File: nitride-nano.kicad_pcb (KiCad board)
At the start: 2 copper layers, 213 parts, among them J1 DX07S024JJ2R1300, J2 61300411121, Q1 EPC2367, Q10 SQJB90EP-T1_GE3, Q11 AO3404A, Q2 EPC2367, Q3 EPC2367, Q4 EPC2367, Q6 AGM612AP, Q7 AO3404A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

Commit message: Fixed the library again
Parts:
- added J3: Conn_01x04_Pin, thommys-parts2:CONN-TH_XT90PW-M.G.Y, F.Cu at (83.0, 80.0)
- added U1: LT8390AIUFD-PBF, thommys-parts2:UFD_28_ADI, F.Cu at (100.8, 63.0)
- moved Q1 1.30 mm to (128.8, 48.8)
- moved Q4 1.30 mm to (128.8, 63.5)
- moved Q2 1.30 mm to (128.8, 53.7)
- moved Q3 1.30 mm to (128.8, 58.6)

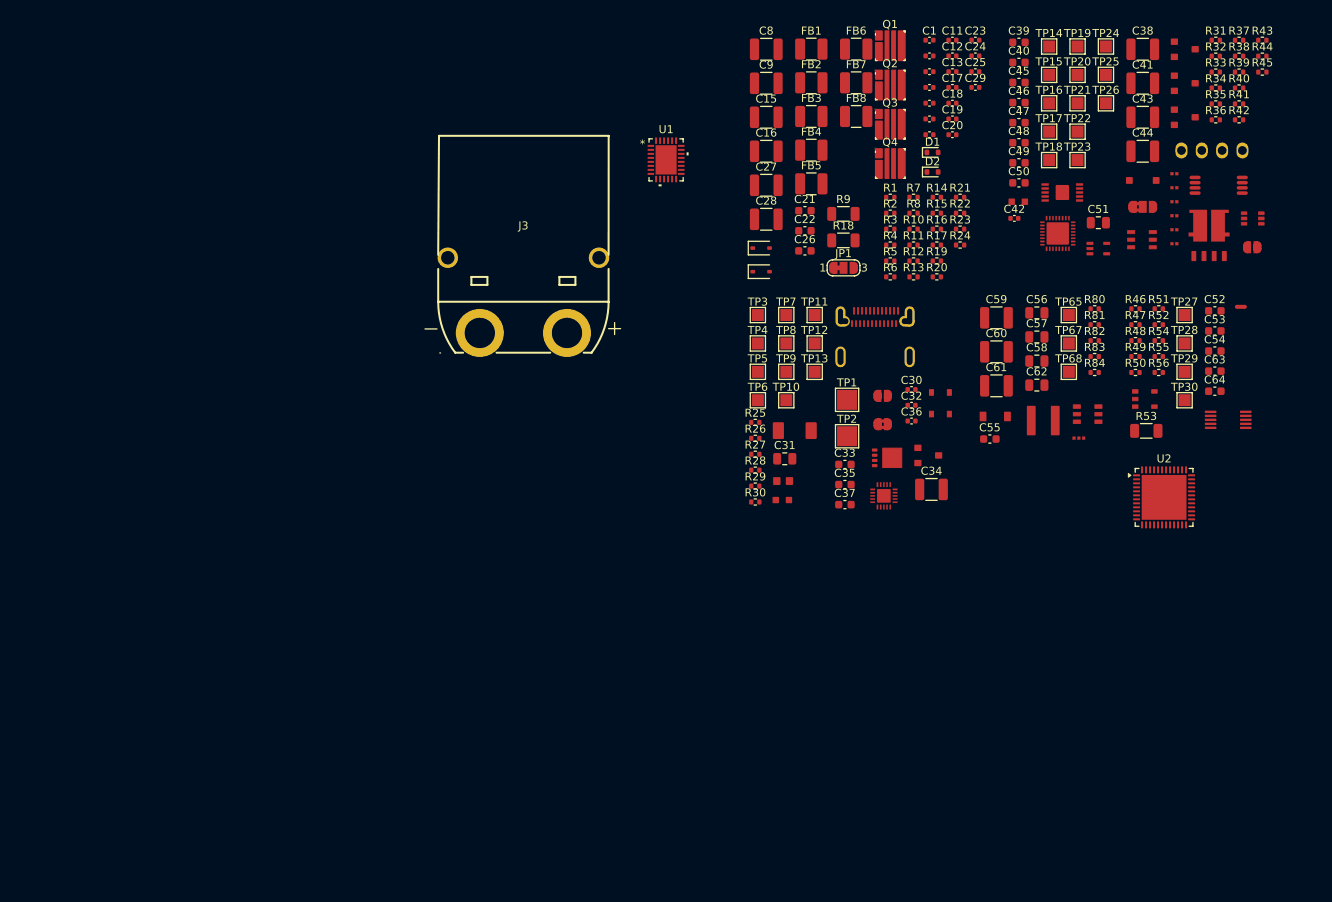
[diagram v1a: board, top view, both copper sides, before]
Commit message: Cleaned up the hierarchy
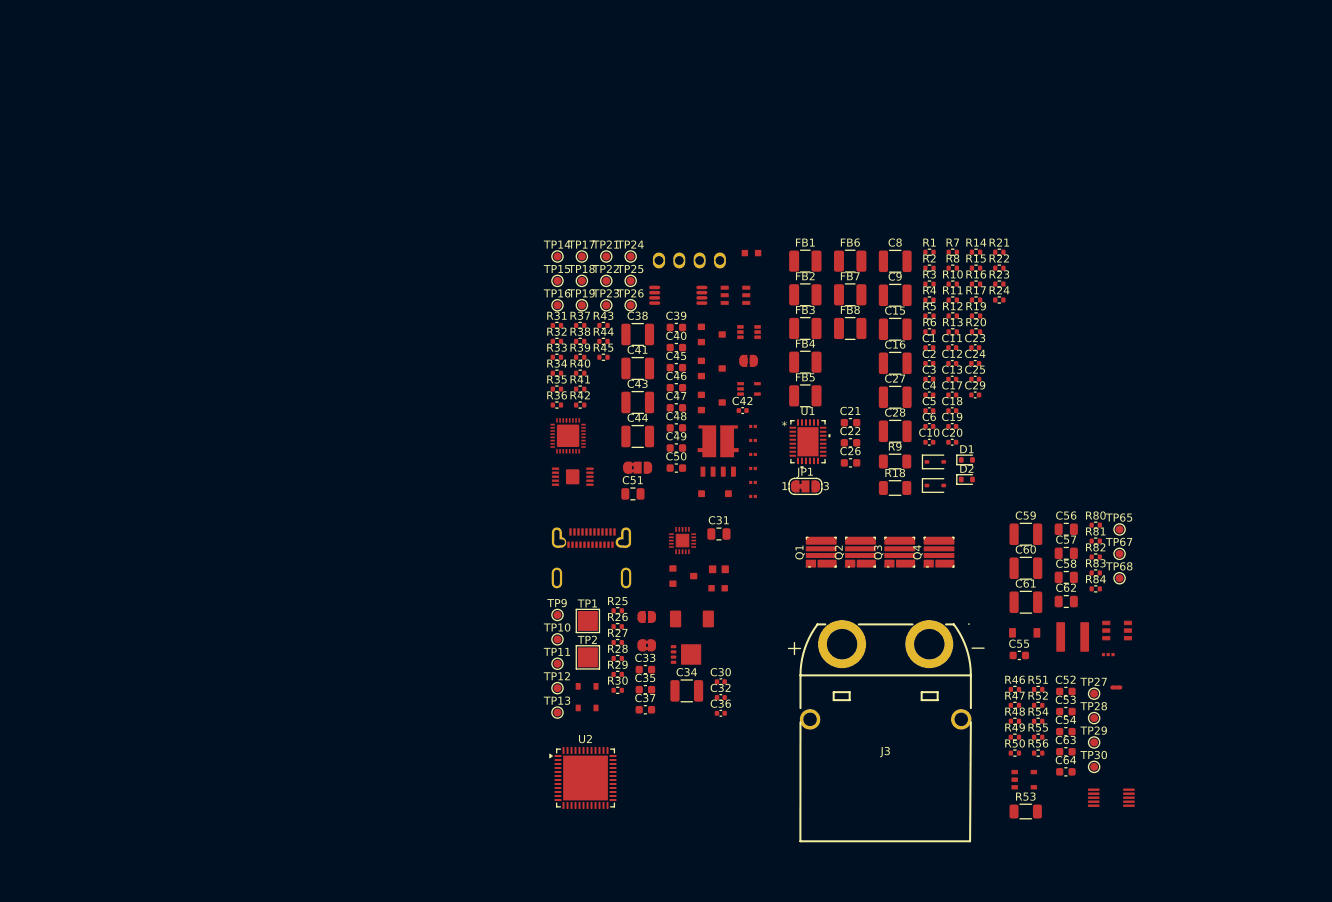
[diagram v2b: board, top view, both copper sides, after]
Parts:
- removed TP20, TP3, TP4, TP5, TP6, TP7, TP8: tp_round_70, TestPoint:TestPoint_Pad_1.5x1.5mm
- TP10, TP11, TP12, TP13, TP14, TP15, TP16, TP17, TP18, TP19, TP21, TP22, TP23, TP24, TP25, TP26, TP27, TP28, TP29, TP30, TP65, TP67, TP68, TP9: footprint TestPoint:TestPoint_Pad_1.5x1.5mm -> TestPoint:TestPoint_Pad_D1.0mm
- moved R37 89.7 mm to (90.1, 83.7)
- moved R38 89.7 mm to (90.1, 85.7)
- moved R39 89.7 mm to (90.1, 87.7)
- moved R40 89.7 mm to (90.1, 89.7)
- moved R41 89.7 mm to (90.1, 91.7)
- moved R42 89.7 mm to (90.1, 93.7)
- moved R43 89.7 mm to (93.0, 83.7)
- moved R44 89.7 mm to (93.0, 85.7)
- moved R45 89.7 mm to (93.0, 87.7)
- moved R31 89.7 mm to (87.2, 83.7)
- moved R32 89.7 mm to (87.2, 85.7)
- moved R33 89.7 mm to (87.2, 87.7)
- moved R34 89.7 mm to (87.2, 89.7)
- moved R35 89.7 mm to (87.2, 91.7)
- moved R36 89.7 mm to (87.2, 93.7)
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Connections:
- net /Converter/CC Set renamed /Converter/CC_Set
- net /Converter/CV Set renamed /Converter/CV_Set
- C29 pad 1: Net-(C29-Pad1) -> /Converter/PWR_REG_OUT
- C6 pad 1: Net-(C6-Pad1) -> /Converter/PWR_UNREG_IN
- FB1 pad 1: Net-(C6-Pad1) -> /Converter/PWR_UNREG_IN
- FB2 pad 1: Net-(C6-Pad1) -> /Converter/PWR_UNREG_IN
- FB3 pad 1: Net-(C6-Pad1) -> /Converter/PWR_UNREG_IN
- FB4 pad 1: Net-(C6-Pad1) -> /Converter/PWR_UNREG_IN
- FB5 pad 2: Net-(C29-Pad1) -> /Converter/PWR_REG_OUT
- FB6 pad 2: Net-(C29-Pad1) -> /Converter/PWR_REG_OUT
- FB7 pad 2: Net-(C29-Pad1) -> /Converter/PWR_REG_OUT
- FB8 pad 2: Net-(C29-Pad1) -> /Converter/PWR_REG_OUT
- J3 pad 2: unconnected-(J3-Pin_2-Pad2) -> /Converter/PWR_REG_OUT
- JP12 pad 1: /LV-Supply/3V3_EN_PD -> /USB-PD/3V3_EN_PD
- Q10 pad 6: +VBUS_SENSED -> /Power-Sense/+VBUS_SENSED
- R53 pad 2: /Power-Sense/+VBUS_OUT -> /Converter/PWR_UNREG_IN
- R54 pad 1: /Power-Sense/+VBUS_OUT -> /Converter/PWR_UNREG_IN
- R55 pad 2: /Power-Sense/SWITCH_EN -> /USB-PD/SWITCH_EN
- TP28 pad 1: /Power-Sense/SWITCH_EN -> /USB-PD/SWITCH_EN
- TP30 pad 1: /Power-Sense/+VBUS_OUT -> /Converter/PWR_UNREG_IN
- TP68 pad 1: /LV-Supply/3V3_EN_PD -> /USB-PD/3V3_EN_PD
- U10 pad 2: /Power-Sense/SWITCH_EN -> /USB-PD/SWITCH_EN
- U9 pad 8: /Power-Sense/+VBUS_OUT -> /Converter/PWR_UNREG_IN

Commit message: inductor, output fets
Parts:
- added D3: PMEG6020EPA,115, PCM_JLCPCB:DFN2020-3_L2.0-W2.0-P0.65-BR-1, F.Cu at (140.3, 110.4)
- added D4: PMEG6020EPA,115, PCM_JLCPCB:DFN2020-3_L2.0-W2.0-P0.65-BR-1, F.Cu at (140.3, 113.7)
- added L1: 1uH, thommys-parts2:IND-SMD_SL1265-101M, F.Cu at (151.2, 98.4)
- added Q12: HUASHUO HSBB0115, thommys-parts2:PRPAK-8_L3.0-W3.0-P0.65-BL-EP, F.Cu at (180.2, 135.9)
- added Q5: HUASHUO HSBB0115, thommys-parts2:PRPAK-8_L3.0-W3.0-P0.65-BL-EP, F.Cu at (175.6, 135.9)
- added R57: 3.3, Resistor_SMD:R_0402_1005Metric, F.Cu at (165.0, 133.3)
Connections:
- R21 pad 2: Net-(Q5-PadG) -> /Converter/LOADTG

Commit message: Starting with layout, oled, encoder, xt90
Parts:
- removed R53: 8m 1%, Resistor_SMD:R_1206_3216Metric
- added C65: 100nF, Capacitor_SMD:C_0402_1005Metric, F.Cu at (122.3, 121.3)
- added C66: 10uF, Capacitor_SMD:C_1210_3225Metric, F.Cu at (145.4, 117.5)
- added C67: 100nF, Capacitor_SMD:C_0402_1005Metric, F.Cu at (122.3, 119.3)
- added C68: 100nF, Capacitor_SMD:C_0402_1005Metric, F.Cu at (122.3, 117.3)
- added C69: 100nF, Capacitor_SMD:C_0402_1005Metric, F.Cu at (122.3, 115.4)
- added C7: 100uF, Capacitor_SMD:CP_Elec_10x12.6, F.Cu at (42.8, 75.3)
- added C70: 10uF, Capacitor_SMD:C_1210_3225Metric, F.Cu at (129.5, 106.6)
- added C71: 100nF, Capacitor_SMD:C_0402_1005Metric, F.Cu at (122.3, 113.4)
- added C72: 100nF, Capacitor_SMD:C_0402_1005Metric, F.Cu at (122.3, 111.4)
- added C73: 100nF, Capacitor_SMD:C_0402_1005Metric, F.Cu at (122.3, 109.5)
- added C74: 100nF, Capacitor_SMD:C_0402_1005Metric, F.Cu at (122.3, 107.5)
- added C75: 15pF, Capacitor_SMD:C_0603_1608Metric, F.Cu at (138.9, 105.5)
- added C76: 15pF, Capacitor_SMD:C_0603_1608Metric, F.Cu at (138.9, 108.0)
- added C77: 10uF, Capacitor_SMD:C_1210_3225Metric, F.Cu at (129.5, 110.8)
- added C78: 100nF, Capacitor_SMD:C_0402_1005Metric, F.Cu at (67.9, 65.1)
- added D15: APTD1608LQBC/D, Altium_port:kingbright_0603_blue, F.Cu at (142.8, 109.3)
- added F1: 10A, Fuse:Fuse_1210_3225Metric, F.Cu at (66.5, 97.2)
- added H1: MountingHole_Pad, MountingHole:MountingHole_3.2mm_M3_Pad_Via, F.Cu at (39.3, 118.6)
- added H2: MountingHole_Pad, MountingHole:MountingHole_3.2mm_M3_Pad_Via, F.Cu at (39.3, 66.0)
- added H3: MountingHole_Pad, MountingHole:MountingHole_3.2mm_M3_Pad_Via, F.Cu at (152.1, 66.0)
- added H4: MountingHole_Pad, MountingHole:MountingHole_3.2mm_M3_Pad_Via, F.Cu at (152.1, 118.8)
- added J4: SWD, Connector:Tag-Connect_TC2030-IDC-NL_2x03_P1.27mm_Vertical, F.Cu at (149.1, 107.5)
- added J5: SSD1306, thommys-parts2:ssd13062, F.Cu at (138.3, 78.8)
- added J6: Conn_01x04_Pin, thommys-parts2:CONN-TH_XT90PW-M, F.Cu at (55.5, 92.1)
- added R58: 330R 1%, Resistor_SMD:R_0402_1005Metric, F.Cu at (142.3, 105.2)
- added R59: 357k, Resistor_SMD:R_0402_1005Metric, F.Cu at (142.3, 107.2)
- added R60: 8mR, Resistor_SMD:R_2512_6332Metric, F.Cu at (66.4, 90.8)
- added SW1: EC11E15244G1, thommys-parts2:RotaryEncoder_Alps_EC11E-Switch_Vertical_H20mm, F.Cu at (115.5, 71.9)
- added U12: FT234XD, Package_DFN_QFN:WDFN-12-1EP_3x3mm_P0.45mm_EP1.7x2.5mm, F.Cu at (129.6, 118.8)
- added Y1: 8M, Crystal:Crystal_SMD_3225-4Pin_3.2x2.5mm, F.Cu at (129.3, 114.2)
- moved TP27 131.4 mm to (45.1, 56.7), turned to 90 degrees
- moved TP28 130.6 mm to (48.2, 56.7), turned to 90 degrees
- moved TP29 130.0 mm to (51.2, 56.7), turned to 90 degrees
- moved TP30 129.5 mm to (54.3, 56.7), turned to 90 degrees
- moved TP65 129.3 mm to (39.0, 57.6), turned to 180 degrees
- moved C64 120.7 mm to (54.7, 66.5), turned to 90 degrees
- moved U10 119.3 mm to (52.0, 66.5), turned to -90 degrees
- moved R55 118.7 mm to (52.5, 63.8), turned to 180 degrees
- moved R56 117.9 mm to (50.6, 69.9), turned to 180 degrees
- moved R50 113.2 mm to (53.5, 69.9), turned to 180 degrees
- moved TP68 112.9 mm to (62.2, 54.8), turned to 180 degrees
- moved U9 111.7 mm to (65.4, 78.0), turned to -90 degrees
- moved TP67 109.7 mm to (62.2, 57.9), turned to 180 degrees
- moved C53 108.7 mm to (59.6, 72.9), turned to 90 degrees
- moved R80 105.7 mm to (58.4, 64.8), turned to 90 degrees
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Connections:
- C52 pad 1: /Power-Sense/V_SENSE -> /MCU/Bus voltage
- C53 pad 1: /Power-Sense/TEMP_SENSE -> /MCU/Temp
- JP8 pad 2: /USB-PD/GPIO15_R -> /MCU/I2CC_SDA_MCU
- JP9 pad 2: /USB-PD/GPIO14_R -> /MCU/I2CC_SCL_MCU
- R26 pad 2: /USB/~{FLT} -> /USB-PD/~{FLT}
- R31 pad 2: /USB-PD/I2C0_SDA -> /Power-Sense/I2C0_SDA
- R32 pad 2: /USB-PD/I2C0_SCL -> /Power-Sense/I2C0_SCL
- R47 pad 2: /Power-Sense/V_SENSE -> /MCU/Bus voltage
- R48 pad 1: /Power-Sense/V_SENSE -> /MCU/Bus voltage
- R50 pad 2: /Power-Sense/TEMP_SENSE -> /MCU/Temp
- R51 pad 1: /Power-Sense/TEMP_SENSE -> /MCU/Temp
- TP11 pad 1: /USB/EPR_EN -> /USB-PD/EPR_EN
- TP12 pad 1: /USB/~{FLT} -> /USB-PD/~{FLT}
- TP27 pad 1: /Power-Sense/V_SENSE -> /MCU/Bus voltage
- U2 pad 1: unconnected-(U2-VBAT-Pad1) -> +3V3
- U2 pad 11: unconnected-(U2-PA3-Pad11) -> /Converter/ISMON
- U2 pad 12: unconnected-(U2-PA4-Pad12) -> /Converter/CV_Set
- U2 pad 14: unconnected-(U2-PA6-Pad14) -> /Converter/CC_Set
- U2 pad 15: unconnected-(U2-PA7-Pad15) -> /MCU/Bus voltage
- U2 pad 16: unconnected-(U2-PC4-Pad16) -> /MCU/I2CC_SDA_MCU
- U2 pad 20: unconnected-(U2-VREF+-Pad20) -> +3V3
- U2 pad 21: unconnected-(U2-VDDA-Pad21) -> +3V3
- U2 pad 23: unconnected-(U2-VDD-Pad23) -> +3V3
- U2 pad 30: unconnected-(U2-PA8-Pad30) -> /MCU/I2CC_SCL_MCU
- U2 pad 31: unconnected-(U2-PA9-Pad31) -> /MCU/Temp
- U2 pad 35: unconnected-(U2-VDD-Pad35) -> +3V3
- U2 pad 36: unconnected-(U2-PA13-Pad36) -> /MCU/SWDIO
- U2 pad 37: unconnected-(U2-PA14-Pad37) -> /MCU/SWCLK
- U2 pad 39: unconnected-(U2-PC10-Pad39) -> Net-(U12-TXD/D0)
- U2 pad 40: unconnected-(U2-PC11-Pad40) -> Net-(U12-RXD/D1)
- U2 pad 46: unconnected-(U2-PB8-Pad46) -> Net-(U2-PB8)
- U2 pad 48: unconnected-(U2-VDD-Pad48) -> +3V3
- U2 pad 49: unconnected-(U2-VSS-Pad49) -> GND
- U2 pad 5: unconnected-(U2-PF0-Pad5) -> Net-(U2-PF0)
- U2 pad 6: unconnected-(U2-PF1-Pad6) -> Net-(U2-PF1)
- U2 pad 7: unconnected-(U2-PG10-Pad7) -> +3V3
- U3 pad 11: /USB/CC2 -> /USB-PD/CC2
- U3 pad 12: /USB/CC1 -> /USB-PD/CC1
- U3 pad 14: /USB/USB_D_N -> /MCU/USB_D_N
- U3 pad 15: /USB/USB_D_P -> /MCU/USB_D_P
- U3 pad 16: /USB/EPR_EN -> /USB-PD/EPR_EN
- U3 pad 9: /USB/~{FLT} -> /USB-PD/~{FLT}
- U4 pad 8: /USB-PD/I2C0_SDA -> /Power-Sense/I2C0_SDA
- U4 pad 9: /USB-PD/I2C0_SCL -> /Power-Sense/I2C0_SCL
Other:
- board outline added: 120 x 60 mm
- board text added: "NITRIDE-NANO"
